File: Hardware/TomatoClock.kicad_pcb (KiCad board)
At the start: 2 copper layers, 50.3 x 31 mm, 26 parts, among them J1 Boot, J2 UART, J3 USB_B_Micro, J4 Ultrasonic, J5 Buttons, J6 Battery, Q1 S9014, U1 STM32F103C8T6, U2 WS4518E, U3 AP1117-33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

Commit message: Hardware: Update PCB and schematics
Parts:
- removed J1: Boot, Connector_PinHeader_2.00mm:PinHeader_2x03_P2.00mm_Vertical
- removed J2: UART, Connector_PinHeader_2.00mm:PinHeader_1x03_P2.00mm_Vertical
- added TP1: BOOT0, TestPoint:TestPoint_Pad_D1.5mm, F.Cu at (105.9, 81.3)
- added TP2: BOOT1, TestPoint:TestPoint_Pad_D1.5mm, F.Cu at (110.5, 81.3)
- added TP3: GND, TestPoint:TestPoint_Pad_D1.5mm, F.Cu at (118.6, 87.6)
- added TP4: VCC, TestPoint:TestPoint_Pad_D1.5mm, F.Cu at (118.6, 98.0)
- added TP5: SWDIO, TestPoint:TestPoint_Pad_D1.5mm, F.Cu at (118.6, 94.7)
- added TP6: SWCLK, TestPoint:TestPoint_Pad_D1.5mm, F.Cu at (118.6, 91.2)
- moved R1 2.34 mm to (102.6, 81.5), turned to 90 degrees
- moved R2 1.37 mm to (114.0, 81.5)
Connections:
- R1 pad 1: Net-(J1-Pad3) -> Net-(R1-Pad1)
- R2 pad 1: BOOT1 -> Net-(R2-Pad1)
- R2 pad 2: Net-(J1-Pad4) -> BOOT1
- U1 pad 20: BOOT1 -> Net-(R2-Pad1)
- U1 pad 30: Net-(J2-Pad1) -> (no net)
- U1 pad 31: Net-(J2-Pad2) -> (no net)
- U1 pad 34: (no net) -> SWDIO
- U1 pad 37: (no net) -> SWCLK
- U1 pad 44: BOOT0 -> Net-(R1-Pad1)
- Y2 pad 3: GND -> (no net)
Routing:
- net Net-(R2-Pad1): track 0.00 -> 19.0 mm, vias 0 -> 2
- net BOOT1: track 15.1 -> 3.79 mm
- net Net-(R1-Pad1): track 0.00 -> 9.73 mm
- net +3V3: track 84.1 -> 76.3 mm, vias 5 -> 4
- net Net-(J1-Pad3): track 7.32 -> 0.00 mm
- net SWCLK: track 0.00 -> 7.30 mm
- net SWDIO: track 0.00 -> 6.87 mm
- net Net-(J1-Pad4): track 6.05 -> 0.00 mm
- net GND: track 183.7 -> 178.3 mm, vias 10 -> 12
- net Net-(J2-Pad2): track 5.11 -> 0.00 mm
- net Net-(J2-Pad1): track 4.49 -> 0.00 mm
- net BOOT0: track 6.97 -> 3.54 mm
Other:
- board text added: "CLK"
- board text added: "DIO"
- board text added: "GND"
- board text added: "VCC"
- board text removed: "0"
- board text removed: "1"
- board text removed: "UART"

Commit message: Hardware: Update hardware
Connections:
- Y2 pad 3: (no net) -> GND
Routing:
- net +3V3: track 76.3 -> 81.9 mm

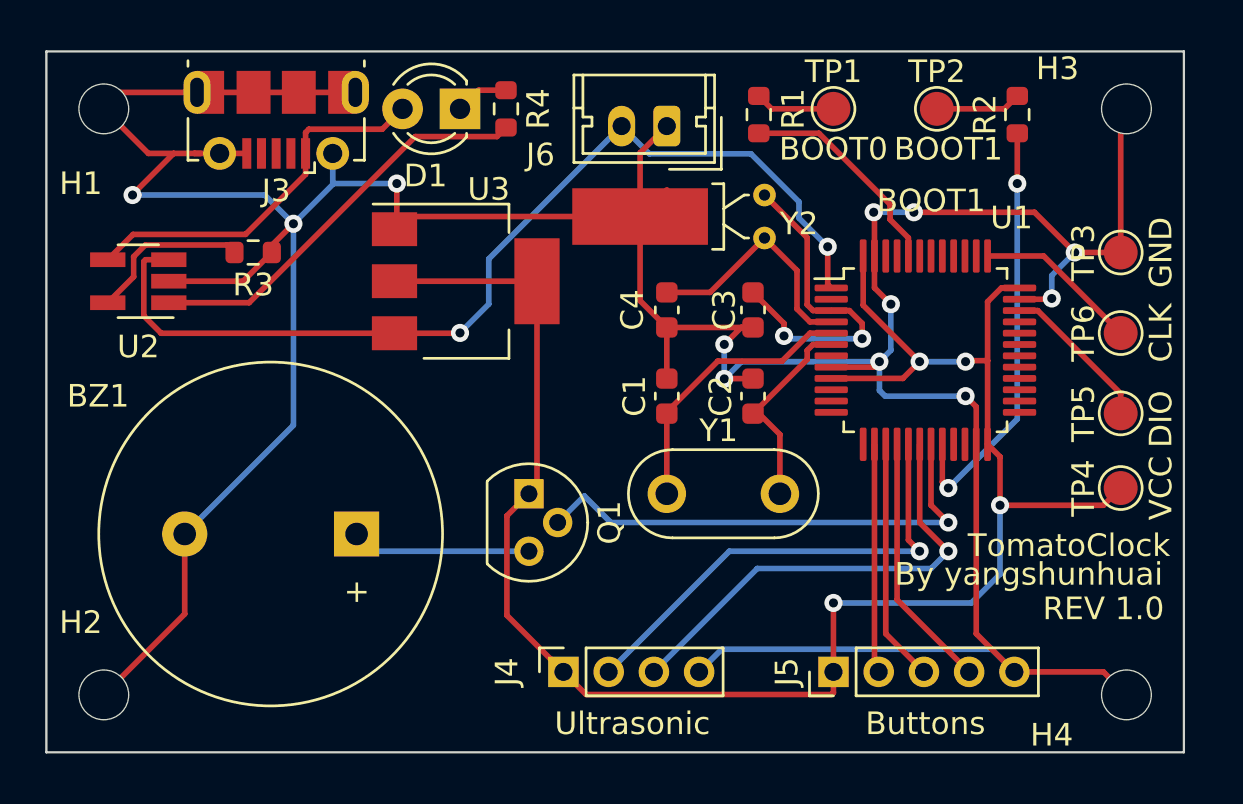
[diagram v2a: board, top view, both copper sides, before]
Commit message: Add copper layer
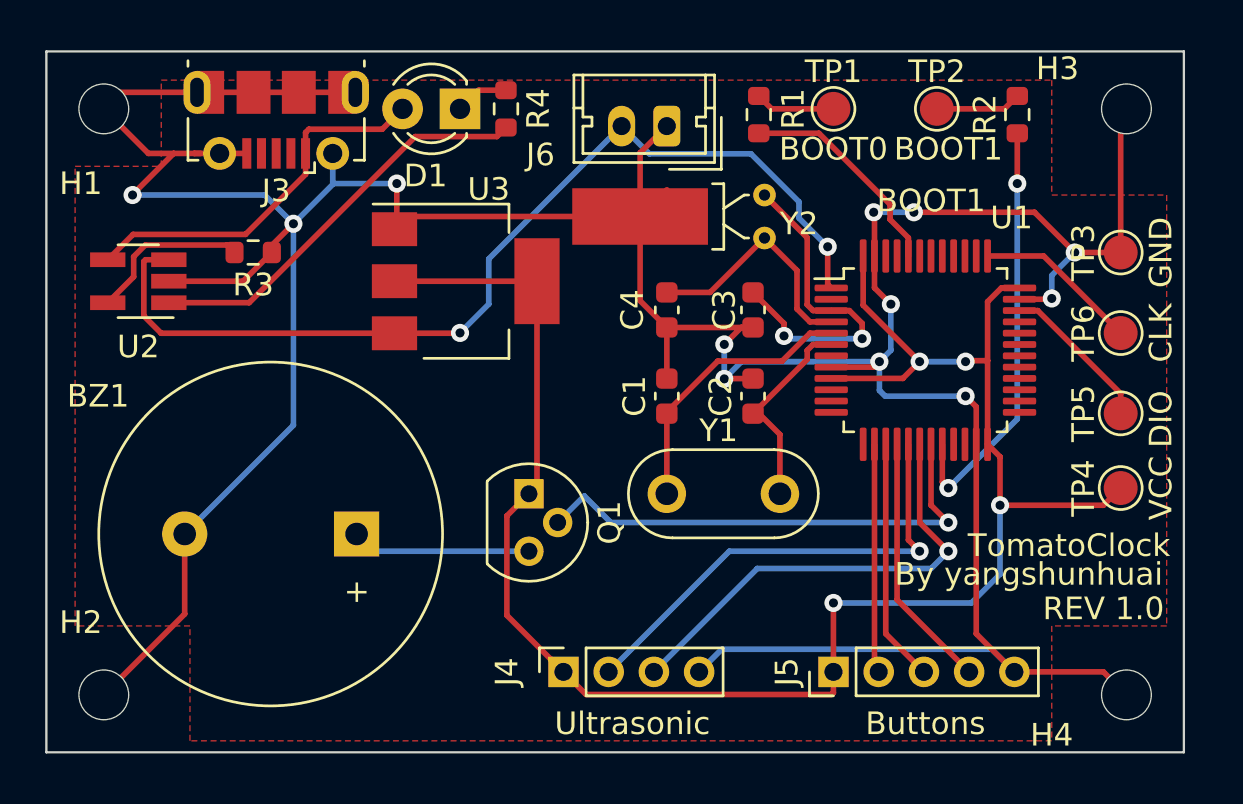
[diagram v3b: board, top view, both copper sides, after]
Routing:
- added copper zone on F.Cu, net GND
